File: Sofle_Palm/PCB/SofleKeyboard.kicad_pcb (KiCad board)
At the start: 2 copper layers, 143.5 x 115.5 mm, 89 parts, among them J1 LED, J2 4PIN, J3 OLED, SW1 SW_PUSH, SW10 SW_PUSH, SW11 SW_PUSH, SW12 SW_PUSH, SW13 SW_PUSH, SW14 SW_PUSH, SW15 SW_PUSH, SW16 SW_PUSH, SW17 SW_PUSH, SW18 SW_PUSH, SW19 SW_PUSH, SW2 SW_PUSH, SW20 SW_PUSH, SW21 SW_PUSH, SW22 SW_PUSH, SW23 SW_PUSH, SW24 SW_PUSH, SW25 Rotary_Encoder_Switch, SW26 SW_PUSH, SW27 SW_PUSH, SW28 SW_PUSH, SW29 SW_PUSH, SW3 SW_PUSH, SW30 SW_PUSH, SW4 SW_PUSH, SW5 SW_PUSH, SW6 SW_PUSH, SW7 SW_PUSH, SW8 SW_PUSH, SW9 SW_PUSH, U1 ProMicro

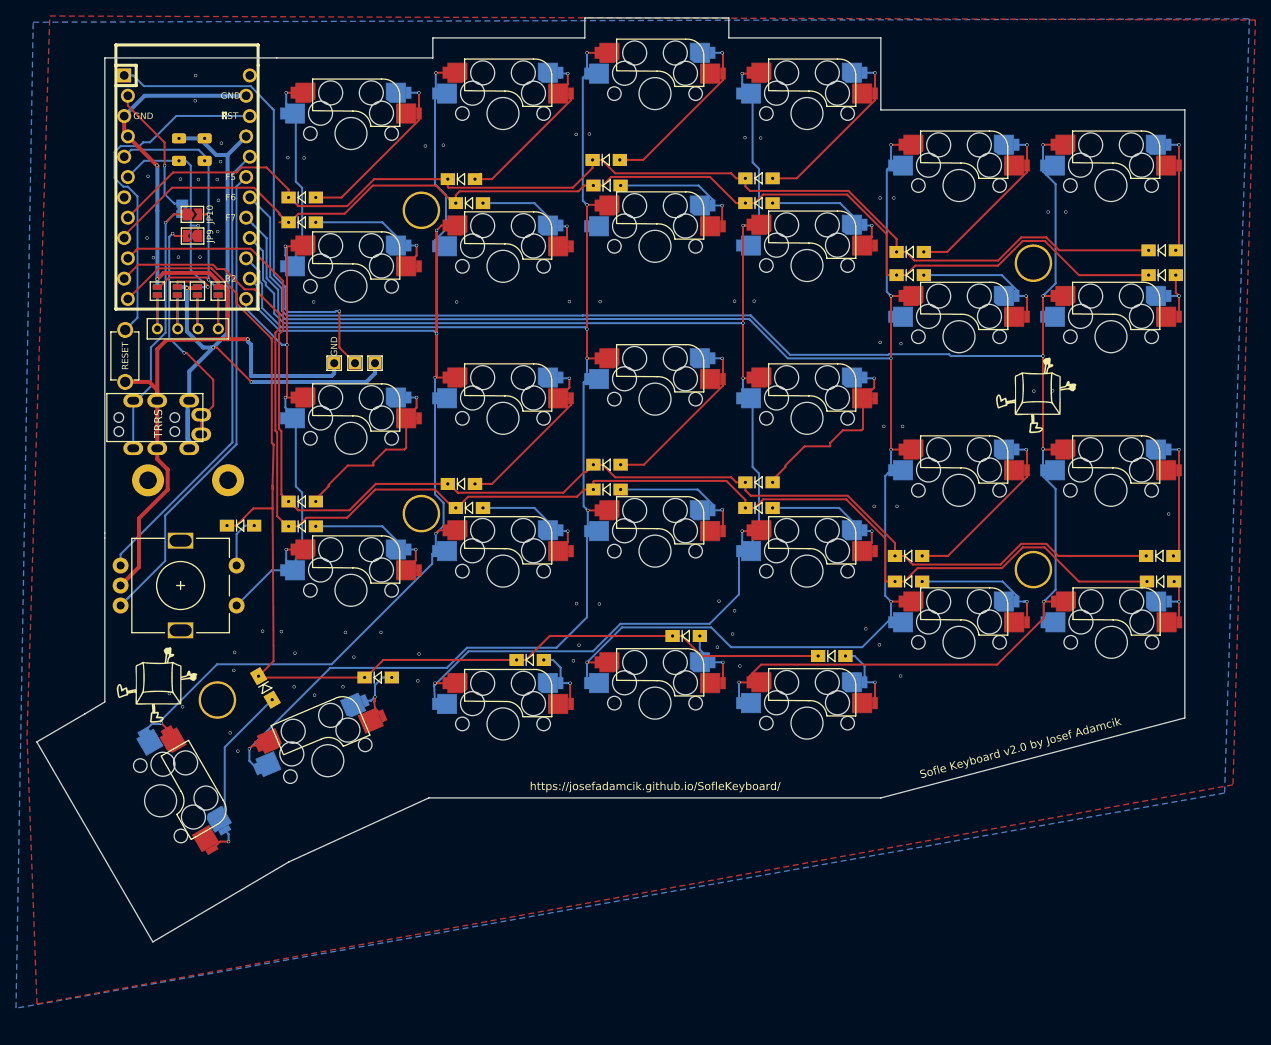
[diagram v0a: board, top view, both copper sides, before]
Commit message: Palm key really added.
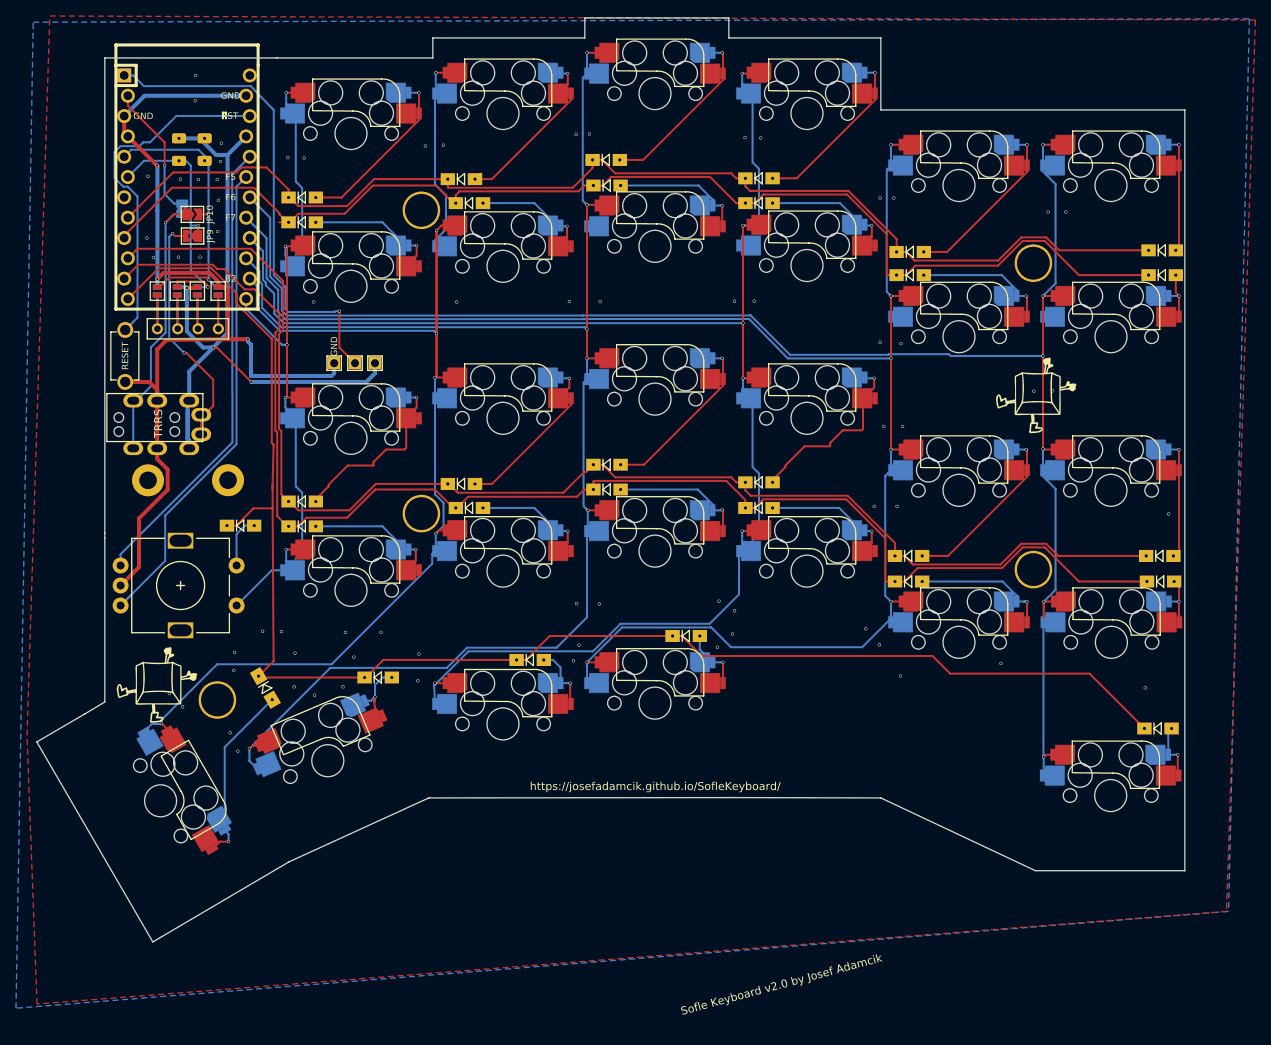
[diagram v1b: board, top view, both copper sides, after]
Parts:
- moved D30 41.8 mm to (221.4, 124.4)
- moved SW30 39.0 mm to (215.5, 132.8)
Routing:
- net row4: track 147.8 -> 192.4 mm
- net col0: track 229.8 -> 205.8 mm
- net GND: vias 73 -> 74
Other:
- outline, holes or cut-outs redrawn

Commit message: Updated PCB for palm key.
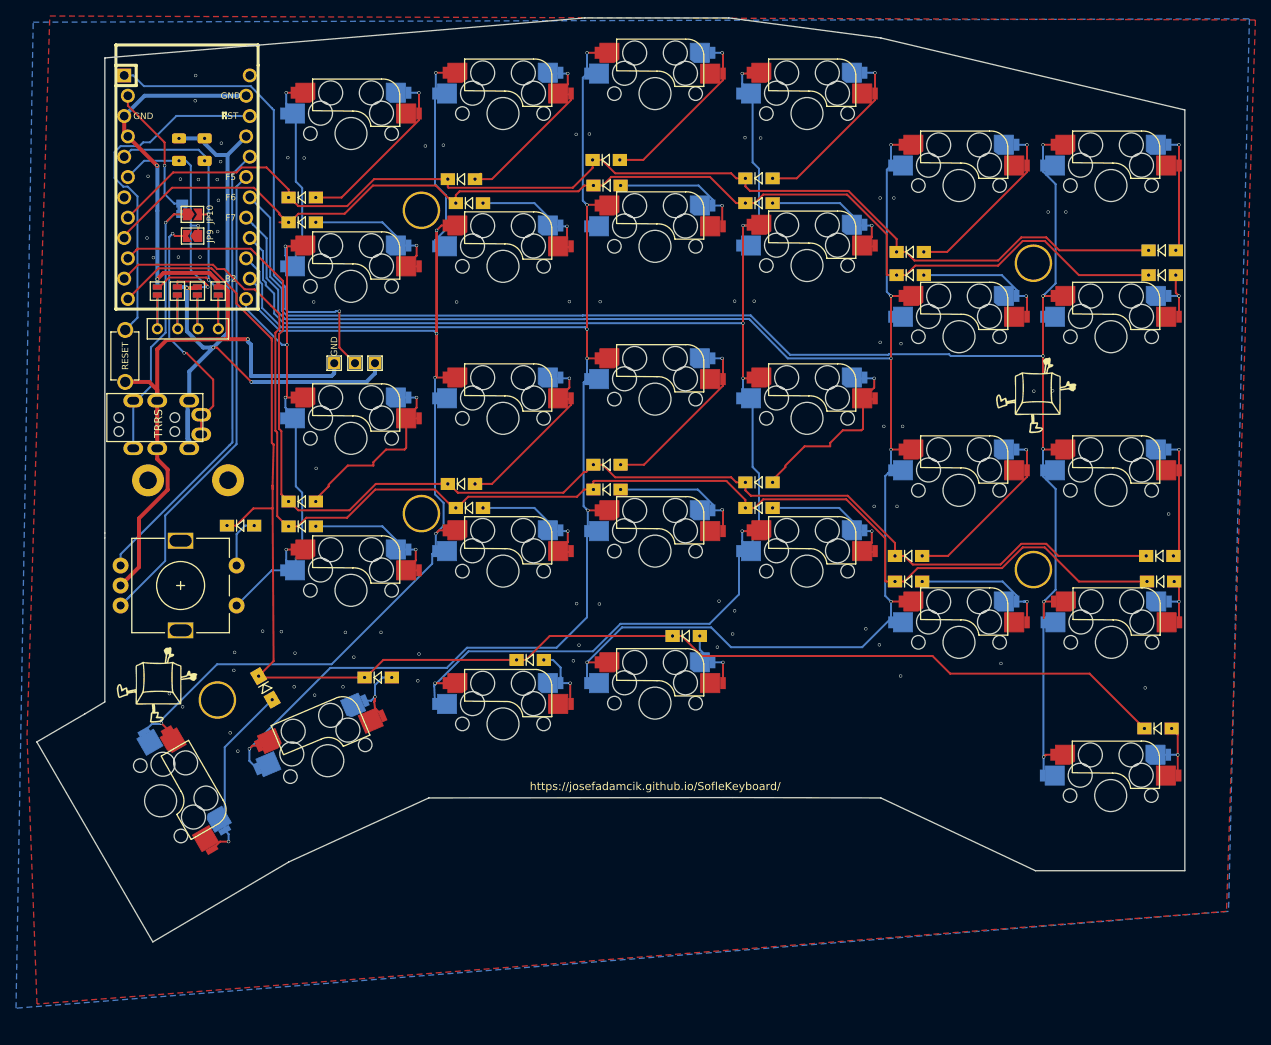
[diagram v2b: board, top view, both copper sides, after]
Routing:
- net Net-(D30-Pad2): track 9.25 -> 10.0 mm
- net GND: vias 74 -> 75
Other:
- outline, holes or cut-outs redrawn
- board text removed: "Sofle Keyboard v2.0 by Josef Adamcik"
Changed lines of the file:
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@@
   (general
     (thickness 1.6)
-    (drawings 31)
-    (tracks 1093)
+    (drawings 23)
+    (tracks 1095)
     (zones 0)
     (modules 89)
@@
       (net 34 GND))
   )
+  (gr_line (start 149.73 35.552) (end 89.73 40.552) (layer Edge.Cuts) (width 0.15))
+  (gr_line (start 186.73 38.052) (end 167.73 35.552) (layer Edge.Cuts) (width 0.15))
+  (gr_line (start 224.73 47.052) (end 186.73 38.052) (layer Edge.Cuts) (width 0.15))
   (gr_line (start 168.216 133.008) (end 186.73 133.052) (layer Edge.Cuts) (width 0.15))
   (gr_line (start 206.062 142.152) (end 224.73 142.152) (layer Edge.Cuts) (width 0.15))
@@
     (effects (font (size 1 1) (thickness 0.15)))
   )
-  (gr_text "Sofle Keyboard v2.0 by Josef Adamcik" (at 173.804 153.582 15) (layer B.SilkS)
-    (effects (font (size 1 1) (thickness 0.15)) (justify mirror))
-  )
-  (gr_text "Sofle Keyboard v2.0 by Josef Adamcik" (at 174.312 156.376 15) (layer F.SilkS)
-    (effects (font (size 1 1) (thickness 0.15)))
-  )
   (gr_line (start 87.1 43.01) (end 87 114.71) (layer Cmts.User) (width 0.15))
   (gr_line (start 87.5 96.21) (end 110.6 96.11) (layer Cmts.User) (width 0.15))
   (gr_circle (center 99.21 106.49) (end 109.16 105.16) (layer Eco1.User) (width 0.15))
   (gr_line (start 45.503294 -44.952764) (end 45.503294 -44.952764) (layer Eco2.User) (width 0.1))
-  (gr_line (start 111.23 40.552) (end 89.73 40.552) (angle 90) (layer Edge.Cuts) (width 0.15))
-  (gr_line (start 130.73 40.552) (end 111.23 40.552) (angle 90) (layer Edge.Cuts) (width 0.15))
-  (gr_line (start 130.73 38.052) (end 130.73 40.552) (angle 90) (layer Edge.Cuts) (width 0.15))
-  (gr_line (start 149.73 38.052) (end 130.73 38.052) (angle 90) (layer Edge.Cuts) (width 0.15))
-  (gr_line (start 149.73 35.552) (end 149.73 38.052) (angle 90) (layer Edge.Cuts) (width 0.15))
   (gr_line (start 167.73 35.552) (end 149.73 35.552) (angle 90) (layer Edge.Cuts) (width 0.15))
-  (gr_line (start 167.73 38.052) (end 167.73 35.552) (angle 90) (layer Edge.Cuts) (width 0.15))
-  (gr_line (start 186.73 38.052) (end 167.73 38.052) (angle 90) (layer Edge.Cuts) (width 0.15))
-  (gr_line (start 186.73 47.052) (end 186.73 38.052) (angle 90) (layer Edge.Cuts) (width 0.15))
-  (gr_line (start 224.73 47.052) (end 186.73 47.052) (angle 90) (layer Edge.Cuts) (width 0.15))
   (gr_line (start 224.73 142.152) (end 224.73 47.052) (angle 90) (layer Edge.Cuts) (width 0.15))
   (gr_line (start 186.73 133.052) (end 206.062 142.152) (angle 90) (layer Edge.Cuts) (width 0.15))
@@
   (via (at 219.778 119.292) (size 0.4) (drill 0.3) (layers F.Cu B.Cu) (net 34))
   (via (at 201.744 116.244) (size 0.4) (drill 0.3) (layers F.Cu B.Cu) (net 34))
+  (via (at 116.146 91.86) (size 0.4) (drill 0.3) (layers F.Cu B.Cu) (net 34))
   (via (at 207.1 108.51) (size 0.4) (drill 0.3) (layers F.Cu B.Cu) (net 35))
   (via (at 207 89.41) (size 0.4) (drill 0.3) (layers F.Cu B.Cu) (net 35))
@@
   (segment (start 223.842 127.674) (end 223.842 130.136) (width 0.25) (layer F.Cu) (net 50))
   (segment (start 222.66 124.792) (end 223.08 124.372) (width 0.25) (layer B.Cu) (net 50))
-  (segment (start 222.66 127.654) (end 222.66 124.792) (width 0.25) (layer B.Cu) (net 50))
+  (segment (start 223.842 125.134) (end 223.08 124.372) (width 0.25) (layer F.Cu) (net 50))
+  (segment (start 223.842 127.674) (end 223.842 125.134) (width 0.25) (layer F.Cu) (net 50))
   (segment (start 106.2 100.06) (end 107.25 99.01) (width 0.25) (layer B.Cu) (net 51))
   (segment (start 107.25 99.01) (end 108.4 99.01) (width 0.25) (layer B.Cu) (net 51))
